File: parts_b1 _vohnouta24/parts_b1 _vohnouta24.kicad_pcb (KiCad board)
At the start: 2 copper layers, 2 parts, among them J1 encoder, J2 SIMSD

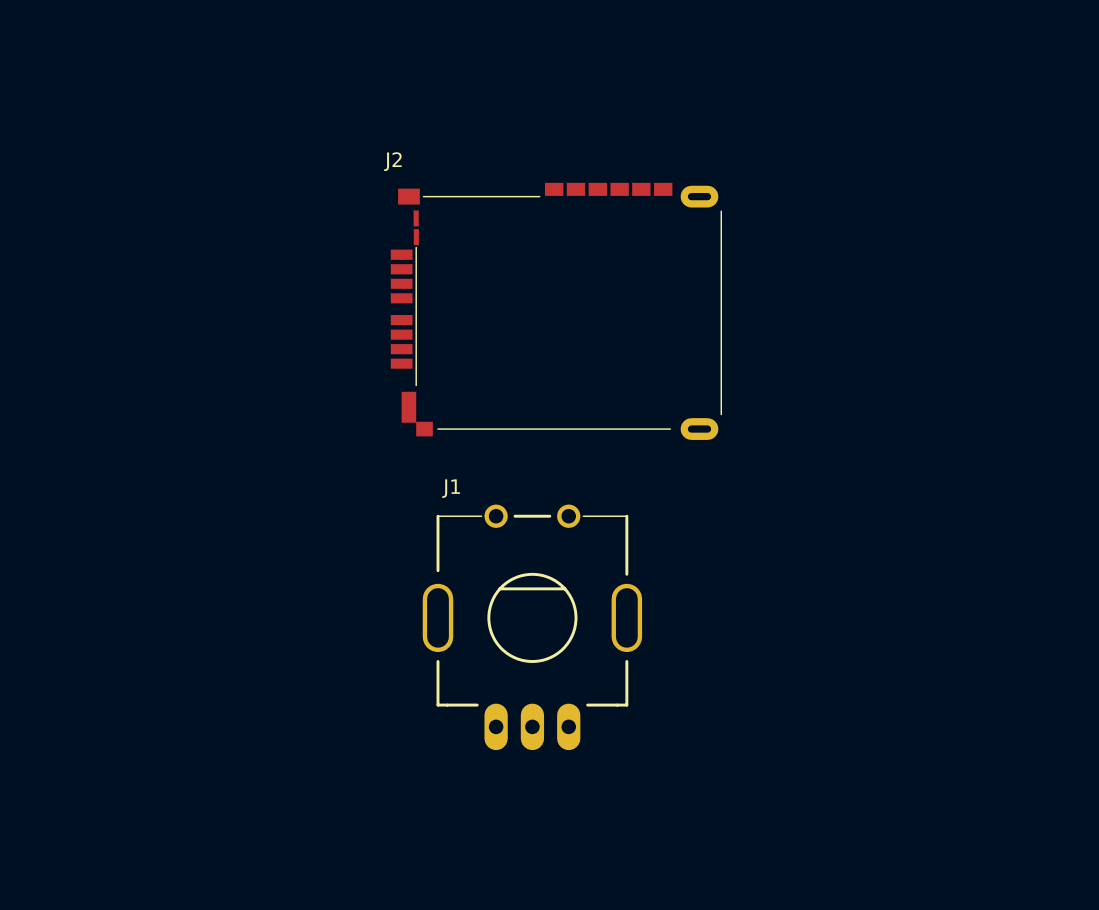
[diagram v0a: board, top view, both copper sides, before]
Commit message: Folders
Re-organized the folders and changed how the library works.
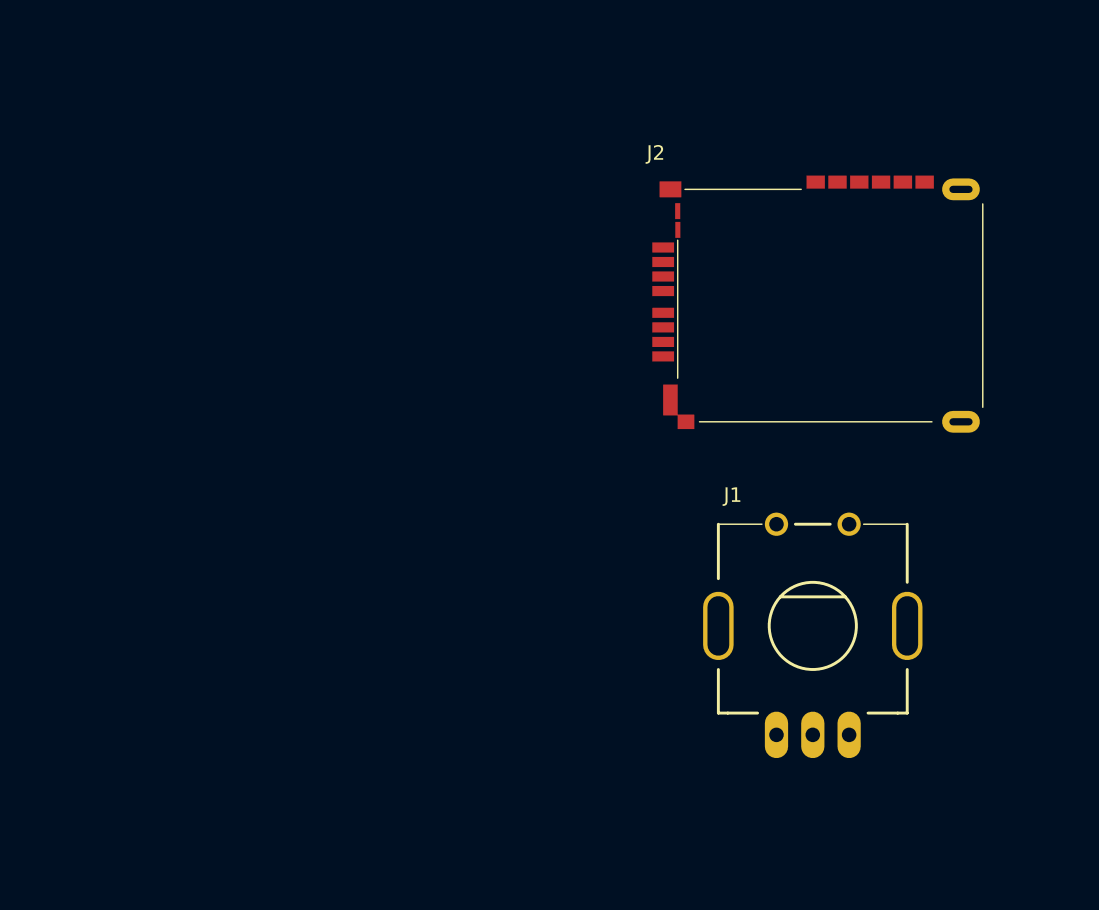
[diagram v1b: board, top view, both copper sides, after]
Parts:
- moved J1 19.3 mm to (171.3, 105.5)
- moved J2 18.0 mm to (169.5, 83.0)
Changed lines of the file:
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@@
 	)
 	(net 0 "")
-	(net 1 "unconnected-(J1-A-Pad1)")
-	(net 2 "unconnected-(J1-B-Pad2)")
-	(net 3 "unconnected-(J1-C-Pad3)")
-	(net 4 "unconnected-(J2-VDD-Pad4)")
-	(net 5 "unconnected-(J2-GND-Pad14)")
-	(net 6 "unconnected-(J2-DAT0-Pad7)")
-	(net 7 "unconnected-(J2-SWITCHB-Pad10)")
-	(net 8 "unconnected-(J2-DAT3-Pad2)")
-	(net 9 "unconnected-(J2-VPP-Pad15)")
+	(net 1 "unconnected-(J1-C-Pad3)")
+	(net 2 "unconnected-(J1-A-Pad1)")
+	(net 3 "unconnected-(J1-B-Pad2)")
+	(net 4 "unconnected-(J2-DAT1-Pad8)")
+	(net 5 "unconnected-(J2-VSS-Pad6)")
+	(net 6 "unconnected-(J2-VCC-Pad11)")
+	(net 7 "unconnected-(J2-DAT3-Pad2)")
+	(net 8 "unconnected-(J2-IO-Pad16)")
+	(net 9 "unconnected-(J2-GND-Pad14)")
 	(net 10 "unconnected-(J2-CLK-Pad5)")
-	(net 11 "unconnected-(J2-CMD-Pad3)")
-	(net 12 "unconnected-(J2-DAT2-Pad1)")
-	(net 13 "unconnected-(J2-IO-Pad16)")
-	(net 14 "unconnected-(J2-DAT1-Pad8)")
-	(net 15 "unconnected-(J2-SWITCHA-Pad9)")
-	(net 16 "unconnected-(J2-RST-Pad12)")
-	(net 17 "unconnected-(J2-VCC-Pad11)")
-	(net 18 "unconnected-(J2-VSS-Pad6)")
-	(net 19 "unconnected-(J2-CLK-Pad13)")
+	(net 11 "unconnected-(J2-VPP-Pad15)")
+	(net 12 "unconnected-(J2-CLK-Pad13)")
+	(net 13 "unconnected-(J2-DAT2-Pad1)")
+	(net 14 "unconnected-(J2-SWITCHA-Pad9)")
+	(net 15 "unconnected-(J2-VDD-Pad4)")
+	(net 16 "unconnected-(J2-CMD-Pad3)")
+	(net 17 "unconnected-(J2-SWITCHB-Pad10)")
+	(net 18 "unconnected-(J2-DAT0-Pad7)")
+	(net 19 "unconnected-(J2-RST-Pad12)")
 	(footprint "parts_b1_vohnouta24:encoder"
 		(layer "F.Cu")
-		(at 152 105)
+		(at 171.3 105.55)
 		(property "Reference" "J1"
 			(at -5.5 -9 0)
@@
 			(layers "*.Cu" "*.Mask")
 			(remove_unused_layers no)
-			(net 1 "unconnected-(J1-A-Pad1)")
+			(net 2 "unconnected-(J1-A-Pad1)")
 			(pinfunction "A")
 			(pintype "passive")
@@
 			(layers "*.Cu" "*.Mask")
 			(remove_unused_layers no)
-			(net 2 "unconnected-(J1-B-Pad2)")
+			(net 3 "unconnected-(J1-B-Pad2)")
 			(pinfunction "B")
 			(pintype "passive")
@@
 			(layers "*.Cu" "*.Mask")
 			(remove_unused_layers no)
-			(net 3 "unconnected-(J1-C-Pad3)")
+			(net 1 "unconnected-(J1-C-Pad3)")
 			(pinfunction "C")
 			(pintype "passive")
@@
 	(footprint "parts_b1_vohnouta24:SIMSD"
 		(layer "F.Cu")
-		(at 151.5 83.5)
+		(at 169.5 83)
 		(property "Reference" "J2"
 			(at -9 -10 0)
@@
 			(size 1.5 0.7)
 			(layers "F.Cu" "F.Mask" "F.Paste")
-			(net 12 "unconnected-(J2-DAT2-Pad1)")
+			(net 13 "unconnected-(J2-DAT2-Pad1)")
 			(pinfunction "DAT2")
 			(pintype "bidirectional")
@@
 			(size 1.5 0.7)
 			(layers "F.Cu" "F.Mask" "F.Paste")
-			(net 8 "unconnected-(J2-DAT3-Pad2)")
+			(net 7 "unconnected-(J2-DAT3-Pad2)")
 			(pinfunction "DAT3")
 			(pintype "bidirectional")
@@
 			(size 1.5 0.7)
 			(layers "F.Cu" "F.Mask" "F.Paste")
-			(net 11 "unconnected-(J2-CMD-Pad3)")
+			(net 16 "unconnected-(J2-CMD-Pad3)")
 			(pinfunction "CMD")
 			(pintype "bidirectional")
@@
 			(size 1.5 0.7)
 			(layers "F.Cu" "F.Mask" "F.Paste")
-			(net 4 "unconnected-(J2-VDD-Pad4)")
+			(net 15 "unconnected-(J2-VDD-Pad4)")
 			(pinfunction "VDD")
 			(pintype "power_in")
@@
 			(size 1.5 0.7)
 			(layers "F.Cu" "F.Mask" "F.Paste")
-			(net 18 "unconnected-(J2-VSS-Pad6)")
+			(net 5 "unconnected-(J2-VSS-Pad6)")
 			(pinfunction "VSS")
 			(pintype "power_in")
@@
 			(size 1.5 0.7)
 			(layers "F.Cu" "F.Mask" "F.Paste")
-			(net 6 "unconnected-(J2-DAT0-Pad7)")
+			(net 18 "unconnected-(J2-DAT0-Pad7)")
 			(pinfunction "DAT0")
 			(pintype "bidirectional")
@@
 			(size 1.5 0.7)
 			(layers "F.Cu" "F.Mask" "F.Paste")
-			(net 14 "unconnected-(J2-DAT1-Pad8)")
+			(net 4 "unconnected-(J2-DAT1-Pad8)")
 			(pinfunction "DAT1")
 			(pintype "bidirectional")
@@
 			(size 1.1 0.35)
 			(layers "F.Cu" "F.Mask" "F.Paste")
-			(net 15 "unconnected-(J2-SWITCHA-Pad9)")
+			(net 14 "unconnected-(J2-SWITCHA-Pad9)")
 			(pinfunction "SWITCHA")
 			(pintype "passive")
@@
 			(size 1.1 0.35)
 			(layers "F.Cu" "F.Mask" "F.Paste")
-			(net 7 "unconnected-(J2-SWITCHB-Pad10)")
+			(net 17 "unconnected-(J2-SWITCHB-Pad10)")
 			(pinfunction "SWITCHB")
 			(pintype "passive")
@@
 			(size 0.9 1.27)
 			(layers "F.Cu" "F.Mask" "F.Paste")
-			(net 17 "unconnected-(J2-VCC-Pad11)")
+			(net 6 "unconnected-(J2-VCC-Pad11)")
 			(pinfunction "VCC")
 			(pintype "power_in")
@@
 			(size 0.9 1.27)
 			(layers "F.Cu" "F.Mask" "F.Paste")
-			(net 16 "unconnected-(J2-RST-Pad12)")
+			(net 19 "unconnected-(J2-RST-Pad12)")
 			(pinfunction "RST")
 			(pintype "bidirectional")
@@
 			(size 0.9 1.27)
 			(layers "F.Cu" "F.Mask" "F.Paste")
-			(net 19 "unconnected-(J2-CLK-Pad13)")
+			(net 12 "unconnected-(J2-CLK-Pad13)")
 			(pinfunction "CLK")
 			(pintype "bidirectional")
@@
 			(size 0.9 1.27)
 			(layers "F.Cu" "F.Mask" "F.Paste")
-			(net 5 "unconnected-(J2-GND-Pad14)")
+			(net 9 "unconnected-(J2-GND-Pad14)")
 			(pinfunction "GND")
 			(pintype "power_in")
@@
 			(size 0.9 1.27)
 			(layers "F.Cu" "F.Mask" "F.Paste")
-			(net 9 "unconnected-(J2-VPP-Pad15)")
+			(net 11 "unconnected-(J2-VPP-Pad15)")
 			(pinfunction "VPP")
 			(pintype "bidirectional")
@@
 			(size 0.9 1.27)
 			(layers "F.Cu" "F.Mask" "F.Paste")
-			(net 13 "unconnected-(J2-IO-Pad16)")
+			(net 8 "unconnected-(J2-IO-Pad16)")
 			(pinfunction "IO")
 			(pintype "bidirectional")

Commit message: Fix
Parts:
- moved J2 42.7 mm to (127.5, 75.5)
- moved J1 42.4 mm to (129.0, 103.0)
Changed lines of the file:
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@@
 	(footprint "parts_b1_vohnouta24:encoder"
 		(layer "F.Cu")
-		(at 171.3 105.55)
+		(at 129 103)
 		(property "Reference" "J1"
-			(at -5.5 -9 0)
+			(at -8.7 -18.45 0)
 			(unlocked yes)
 			(layer "F.SilkS")
@@
 		)
 		(property "Value" "encoder"
-			(at 4.5 -9 0)
+			(at 1.3 -18.45 0)
 			(unlocked yes)
 			(layer "F.Fab")
@@
 			(end -3.5 -7)
 			(stroke
-				(width 0.1)
-				(type default)
+				(width 0.2)
+				(type solid)
 			)
 			(layer "F.SilkS")
@@
 			(end 3.5 -7)
 			(stroke
-				(width 0.1)
-				(type default)
+				(width 0.2)
+				(type solid)
 			)
 			(layer "F.SilkS")
@@
 	(footprint "parts_b1_vohnouta24:SIMSD"
 		(layer "F.Cu")
-		(at 169.5 83)
+		(at 127.5 75.5)
 		(property "Reference" "J2"
 			(at -9 -10 0)

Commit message: bub fix (yes)
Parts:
- moved J2 50.6 mm to (175.4, 91.7)
- moved J1 50.2 mm to (178.0, 114.0)
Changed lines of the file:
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@@
 	)
 	(net 0 "")
-	(net 1 "unconnected-(J1-C-Pad3)")
-	(net 2 "unconnected-(J1-A-Pad1)")
+	(net 1 "unconnected-(J1-A-Pad1)")
+	(net 2 "unconnected-(J1-C-Pad3)")
 	(net 3 "unconnected-(J1-B-Pad2)")
-	(net 4 "unconnected-(J2-DAT1-Pad8)")
-	(net 5 "unconnected-(J2-VSS-Pad6)")
-	(net 6 "unconnected-(J2-VCC-Pad11)")
-	(net 7 "unconnected-(J2-DAT3-Pad2)")
-	(net 8 "unconnected-(J2-IO-Pad16)")
-	(net 9 "unconnected-(J2-GND-Pad14)")
+	(net 4 "unconnected-(J2-IO-Pad16)")
+	(net 5 "unconnected-(J2-SWITCHA-Pad9)")
+	(net 6 "unconnected-(J2-DAT2-Pad1)")
+	(net 7 "unconnected-(J2-VSS-Pad6)")
+	(net 8 "unconnected-(J2-RST-Pad12)")
+	(net 9 "unconnected-(J2-CLK-Pad13)")
 	(net 10 "unconnected-(J2-CLK-Pad5)")
-	(net 11 "unconnected-(J2-VPP-Pad15)")
-	(net 12 "unconnected-(J2-CLK-Pad13)")
-	(net 13 "unconnected-(J2-DAT2-Pad1)")
-	(net 14 "unconnected-(J2-SWITCHA-Pad9)")
-	(net 15 "unconnected-(J2-VDD-Pad4)")
-	(net 16 "unconnected-(J2-CMD-Pad3)")
-	(net 17 "unconnected-(J2-SWITCHB-Pad10)")
-	(net 18 "unconnected-(J2-DAT0-Pad7)")
-	(net 19 "unconnected-(J2-RST-Pad12)")
+	(net 11 "unconnected-(J2-DAT0-Pad7)")
+	(net 12 "unconnected-(J2-VCC-Pad11)")
+	(net 13 "unconnected-(J2-CMD-Pad3)")
+	(net 14 "unconnected-(J2-DAT3-Pad2)")
+	(net 15 "unconnected-(J2-GND-Pad14)")
+	(net 16 "unconnected-(J2-SWITCHB-Pad10)")
+	(net 17 "unconnected-(J2-VPP-Pad15)")
+	(net 18 "unconnected-(J2-VDD-Pad4)")
+	(net 19 "unconnected-(J2-DAT1-Pad8)")
 	(footprint "parts_b1_vohnouta24:encoder"
 		(layer "F.Cu")
-		(at 129 103)
+		(at 178 114)
 		(property "Reference" "J1"
-			(at -8.7 -18.45 0)
+			(at -5.5 -9 0)
 			(unlocked yes)
 			(layer "F.SilkS")
@@
 		)
 		(property "Value" "encoder"
-			(at 1.3 -18.45 0)
+			(at 4.5 -9 0)
 			(unlocked yes)
 			(layer "F.Fab")
@@
 			(layers "*.Cu" "*.Mask")
 			(remove_unused_layers no)
-			(net 2 "unconnected-(J1-A-Pad1)")
+			(net 1 "unconnected-(J1-A-Pad1)")
 			(pinfunction "A")
 			(pintype "passive")
@@
 			(layers "*.Cu" "*.Mask")
 			(remove_unused_layers no)
-			(net 1 "unconnected-(J1-C-Pad3)")
+			(net 2 "unconnected-(J1-C-Pad3)")
 			(pinfunction "C")
 			(pintype "passive")
@@
 	(footprint "parts_b1_vohnouta24:SIMSD"
 		(layer "F.Cu")
-		(at 127.5 75.5)
+		(at 175.45 91.65)
 		(property "Reference" "J2"
 			(at -9 -10 0)
@@
 		)
 		(property "Value" "SIMSD"
-			(at -7.5 11 0)
+			(at -3.5 15.5 0)
 			(unlocked yes)
 			(layer "F.Fab")
@@
 			(layer "F.SilkS")
 		)
+		(pad "" smd rect
+			(at -8 -7.5)
+			(size 1.5 1.1)
+			(layers "F.Cu" "F.Mask" "F.Paste")
+		)
+		(pad "" smd rect
+			(at -8 7)
+			(size 1 2.13)
+			(layers "F.Cu" "F.Mask" "F.Paste")
+		)
+		(pad "" smd rect
+			(at -6.93 8.5)
+			(size 1.15 1)
+			(layers "F.Cu" "F.Mask" "F.Paste")
+		)
+		(pad "" thru_hole oval
+			(at 12 -7.5)
+			(size 2.15 1.1)
+			(drill oval 1.6 0.5)
+			(layers "*.Cu" "*.Mask")
+			(remove_unused_layers no)
+		)
+		(pad "" thru_hole oval
+			(at 12 8.5)
+			(size 2.15 1.1)
+			(drill oval 1.6 0.5)
+			(layers "*.Cu" "*.Mask")
+			(remove_unused_layers no)
+		)
 		(pad "1" smd rect
 			(at -8.5 -3.5 180)
-			(size 1.5 0.7)
-			(layers "F.Cu" "F.Mask" "F.Paste")
-			(net 13 "unconnected-(J2-DAT2-Pad1)")
+			(size 1 0.7)
+			(layers "F.Cu" "F.Mask" "F.Paste")
+			(net 6 "unconnected-(J2-DAT2-Pad1)")
 			(pinfunction "DAT2")
 			(pintype "bidirectional")
@@
 		(pad "2" smd rect
 			(at -8.5 -2.5 180)
-			(size 1.5 0.7)
-			(layers "F.Cu" "F.Mask" "F.Paste")
-			(net 7 "unconnected-(J2-DAT3-Pad2)")
+			(size 1 0.7)
+			(layers "F.Cu" "F.Mask" "F.Paste")
+			(net 14 "unconnected-(J2-DAT3-Pad2)")
 			(pinfunction "DAT3")
 			(pintype "bidirectional")
@@
 		(pad "3" smd rect
 			(at -8.5 -1.5 180)
-			(size 1.5 0.7)
-			(layers "F.Cu" "F.Mask" "F.Paste")
-			(net 16 "unconnected-(J2-CMD-Pad3)")
+			(size 1 0.7)
+			(layers "F.Cu" "F.Mask" "F.Paste")
+			(net 13 "unconnected-(J2-CMD-Pad3)")
 			(pinfunction "CMD")
 			(pintype "bidirectional")
@@
 		(pad "4" smd rect
 			(at -8.5 -0.5 180)
-			(size 1.5 0.7)
-			(layers "F.Cu" "F.Mask" "F.Paste")
-			(net 15 "unconnected-(J2-VDD-Pad4)")
+			(size 1 0.7)
+			(layers "F.Cu" "F.Mask" "F.Paste")
+			(net 18 "unconnected-(J2-VDD-Pad4)")
 			(pinfunction "VDD")
 			(pintype "power_in")
@@
 		(pad "5" smd rect
 			(at -8.5 1 180)
-			(size 1.5 0.7)
+			(size 1 0.7)
 			(layers "F.Cu" "F.Mask" "F.Paste")
 			(net 10 "unconnected-(J2-CLK-Pad5)")
@@
 		(pad "6" smd rect
 			(at -8.5 2 180)
-			(size 1.5 0.7)
-			(layers "F.Cu" "F.Mask" "F.Paste")
-			(net 5 "unconnected-(J2-VSS-Pad6)")
+			(size 1 0.7)
+			(layers "F.Cu" "F.Mask" "F.Paste")
+			(net 7 "unconnected-(J2-VSS-Pad6)")
 			(pinfunction "VSS")
 			(pintype "power_in")
@@
 		(pad "7" smd rect
 			(at -8.5 3 180)
-			(size 1.5 0.7)
-			(layers "F.Cu" "F.Mask" "F.Paste")
-			(net 18 "unconnected-(J2-DAT0-Pad7)")
+			(size 1 0.7)
+			(layers "F.Cu" "F.Mask" "F.Paste")
+			(net 11 "unconnected-(J2-DAT0-Pad7)")
 			(pinfunction "DAT0")
 			(pintype "bidirectional")
@@
 		(pad "8" smd rect
 			(at -8.5 4 180)
-			(size 1.5 0.7)
-			(layers "F.Cu" "F.Mask" "F.Paste")
-			(net 4 "unconnected-(J2-DAT1-Pad8)")
+			(size 1 0.7)
+			(layers "F.Cu" "F.Mask" "F.Paste")
+			(net 19 "unconnected-(J2-DAT1-Pad8)")
 			(pinfunction "DAT1")
 			(pintype "bidirectional")
@@
 		(pad "9" smd rect
 			(at -7.5 -6 270)
-			(size 1.1 0.35)
-			(layers "F.Cu" "F.Mask" "F.Paste")
-			(net 14 "unconnected-(J2-SWITCHA-Pad9)")
+			(size 1 0.6)
+			(layers "F.Cu" "F.Mask" "F.Paste")
+			(net 5 "unconnected-(J2-SWITCHA-Pad9)")
 			(pinfunction "SWITCHA")
 			(pintype "passive")
@@
 		(pad "10" smd rect
 			(at -7.49 -4.71 270)
-			(size 1.1 0.35)
-			(layers "F.Cu" "F.Mask" "F.Paste")
-			(net 17 "unconnected-(J2-SWITCHB-Pad10)")
+			(size 1 0.6)
+			(layers "F.Cu" "F.Mask" "F.Paste")
+			(net 16 "unconnected-(J2-SWITCHB-Pad10)")
 			(pinfunction "SWITCHB")
 			(pintype "passive")
@@
 		(pad "11" smd rect
 			(at 9.5 -8 270)
-			(size 0.9 1.27)
-			(layers "F.Cu" "F.Mask" "F.Paste")
-			(net 6 "unconnected-(J2-VCC-Pad11)")
+			(size 0.9 1.1)
+			(layers "F.Cu" "F.Mask" "F.Paste")
+			(net 12 "unconnected-(J2-VCC-Pad11)")
 			(pinfunction "VCC")
 			(pintype "power_in")
@@
 		(pad "12" smd rect
 			(at 6.5 -8 270)
-			(size 0.9 1.27)
-			(layers "F.Cu" "F.Mask" "F.Paste")
-			(net 19 "unconnected-(J2-RST-Pad12)")
+			(size 0.9 1.1)
+			(layers "F.Cu" "F.Mask" "F.Paste")
+			(net 8 "unconnected-(J2-RST-Pad12)")
 			(pinfunction "RST")
 			(pintype "bidirectional")
@@
 		(pad "13" smd rect
 			(at 3.5 -8 270)
-			(size 0.9 1.27)
-			(layers "F.Cu" "F.Mask" "F.Paste")
-			(net 12 "unconnected-(J2-CLK-Pad13)")
+			(size 0.9 1.1)
+			(layers "F.Cu" "F.Mask" "F.Paste")
+			(net 9 "unconnected-(J2-CLK-Pad13)")
 			(pinfunction "CLK")
 			(pintype "bidirectional")
@@
 		(pad "14" smd rect
 			(at 8 -8 270)
-			(size 0.9 1.27)
-			(layers "F.Cu" "F.Mask" "F.Paste")
-			(net 9 "unconnected-(J2-GND-Pad14)")
+			(size 0.9 1.1)
+			(layers "F.Cu" "F.Mask" "F.Paste")
+			(net 15 "unconnected-(J2-GND-Pad14)")
 			(pinfunction "GND")
 			(pintype "power_in")
@@
 		(pad "15" smd rect
 			(at 5 -8 270)
-			(size 0.9 1.27)
-			(layers "F.Cu" "F.Mask" "F.Paste")
-			(net 11 "unconnected-(J2-VPP-Pad15)")
+			(size 0.9 1.1)
+			(layers "F.Cu" "F.Mask" "F.Paste")
+			(net 17 "unconnected-(J2-VPP-Pad15)")
 			(pinfunction "VPP")
 			(pintype "bidirectional")
@@
 		(pad "16" smd rect
 			(at 2 -8 270)
-			(size 0.9 1.27)
-			(layers "F.Cu" "F.Mask" "F.Paste")
-			(net 8 "unconnected-(J2-IO-Pad16)")
+			(size 0.9 1.1)
+			(layers "F.Cu" "F.Mask" "F.Paste")
+			(net 4 "unconnected-(J2-IO-Pad16)")
 			(pinfunction "IO")
 			(pintype "bidirectional")
 		)
-		(pad "SH" smd rect
-			(at -8 -7.5)
-			(size 1.5 1.1)
-			(layers "F.Cu" "F.Mask" "F.Paste")
-		)
-		(pad "SH" smd rect
-			(at -8 7)
-			(size 1 2.13)
-			(layers "F.Cu" "F.Mask" "F.Paste")
-		)
-		(pad "SH" smd rect
-			(at -6.93 8.5)
-			(size 1.15 1)
-			(layers "F.Cu" "F.Mask" "F.Paste")
-		)
-		(pad "SH" thru_hole oval
-			(at 12 -7.5)
-			(size 2.6 1.5)
-			(drill oval 1.6 0.5)
-			(layers "*.Cu" "*.Mask")
-			(remove_unused_layers no)
-		)
-		(pad "SH" thru_hole oval
-			(at 12 8.5)
-			(size 2.6 1.5)
-			(drill oval 1.6 0.5)
-			(layers "*.Cu" "*.Mask")
-			(remove_unused_layers no)
-		)
 		(embedded_fonts no)
